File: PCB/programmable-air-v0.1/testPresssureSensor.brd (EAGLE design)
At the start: 43.2 x 35.2 mm, 6 parts, among them J1 4p-2.54

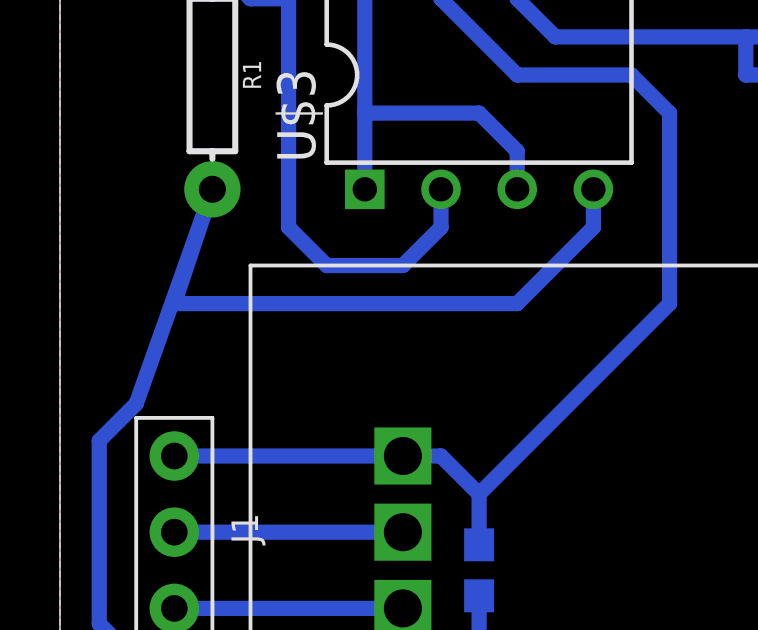
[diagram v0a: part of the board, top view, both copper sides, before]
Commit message: Added clearance for easier production
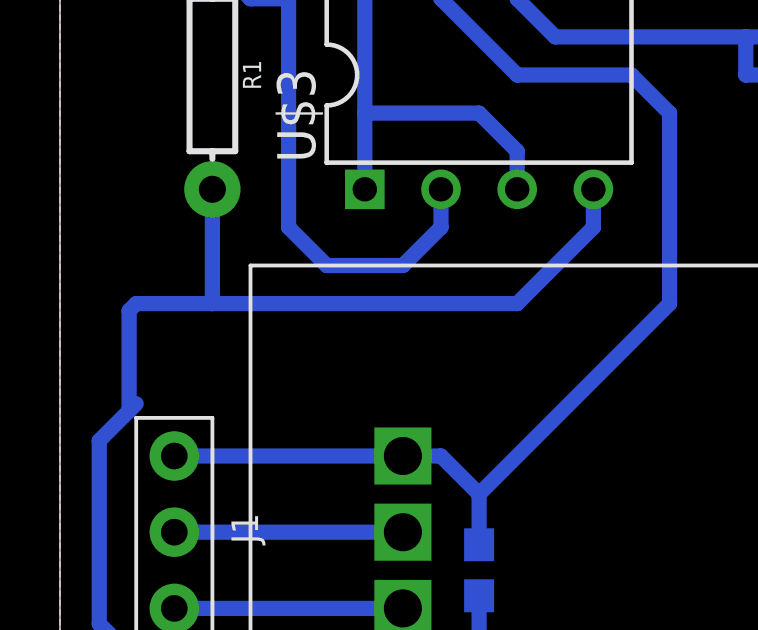
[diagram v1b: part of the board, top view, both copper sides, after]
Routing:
- net GND: track 51.4 -> 48.5 mm
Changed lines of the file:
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@@
 <param name="mtCopper" value="0.035mm 0.035mm 0.035mm 0.035mm 0.035mm 0.035mm 0.035mm 0.035mm 0.035mm 0.035mm 0.035mm 0.035mm 0.035mm 0.035mm 0.035mm 0.035mm"/>
 <param name="mtIsolate" value="1.5mm 0.15mm 0.2mm 0.15mm 0.2mm 0.15mm 0.2mm 0.15mm 0.2mm 0.15mm 0.2mm 0.15mm 0.2mm 0.15mm 0.2mm"/>
-<param name="mdWireWire" value="12mil"/>
-<param name="mdWirePad" value="12mil"/>
-<param name="mdWireVia" value="12mil"/>
-<param name="mdPadPad" value="12mil"/>
-<param name="mdPadVia" value="12mil"/>
-<param name="mdViaVia" value="12mil"/>
-<param name="mdSmdPad" value="12mil"/>
-<param name="mdSmdVia" value="12mil"/>
-<param name="mdSmdSmd" value="12mil"/>
+<param name="mdWireWire" value="20mil"/>
+<param name="mdWirePad" value="20mil"/>
+<param name="mdWireVia" value="20mil"/>
+<param name="mdPadPad" value="20mil"/>
+<param name="mdPadVia" value="20mil"/>
+<param name="mdViaVia" value="20mil"/>
+<param name="mdSmdPad" value="20mil"/>
+<param name="mdSmdVia" value="20mil"/>
+<param name="mdSmdSmd" value="20mil"/>
 <param name="mdViaViaSameLayer" value="6mil"/>
 <param name="mnLayersViaInSmd" value="2"/>
@@
 <wire x1="3.81" y1="7.62" x2="11.43" y2="7.62" width="0.508" layer="16"/>
 <wire x1="3.81" y1="7.62" x2="2.54" y2="8.417825" width="0.508" layer="16"/>
-<wire x1="2.54" y1="16.982175" x2="5.08" y2="24.13" width="0.508" layer="16"/>
 <wire x1="2.54" y1="8.417825" x2="1.3081" y2="9.649725" width="0.508" layer="16"/>
-<wire x1="1.3081" y1="15.750275" x2="2.54" y2="16.982175" width="0.508" layer="16"/>
+<wire x1="1.3081" y1="15.750275" x2="2.3039125" y2="16.7460875" width="0.508" layer="16"/>
+<wire x1="2.3039125" y1="16.7460875" x2="2.54" y2="16.982175" width="0.508" layer="16"/>
 <wire x1="1.3081" y1="9.649725" x2="1.3081" y2="15.750275" width="0.508" layer="16"/>
-<wire x1="5.08" y1="24.13" x2="3.81" y2="20.32" width="0.508" layer="16"/>
-<wire x1="3.81" y1="20.32" x2="15.24" y2="20.32" width="0.508" layer="16"/>
 <wire x1="17.78" y1="22.86" x2="17.78" y2="24.13" width="0.508" layer="16"/>
 <wire x1="15.24" y1="20.32" x2="17.78" y2="22.86" width="0.508" layer="16"/>
@@
 <vertex x="0" y="0"/>
 </polygon>
+<wire x1="2.3039125" y1="16.7460875" x2="2.3039125" y2="20.0839125" width="0.508" layer="16"/>
+<wire x1="2.3039125" y1="20.0839125" x2="2.54" y2="20.32" width="0.508" layer="16"/>
+<wire x1="2.54" y1="20.32" x2="5.08" y2="20.32" width="0.508" layer="16"/>
+<wire x1="5.08" y1="20.32" x2="5.08" y2="24.13" width="0.508" layer="16"/>
+<wire x1="5.08" y1="20.32" x2="15.24" y2="20.32" width="0.508" layer="16"/>
 </signal>
 <signal name="N$1">
